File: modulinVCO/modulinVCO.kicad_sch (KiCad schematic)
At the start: 106 parts, among them J1 Conn_01x06_Pin, Q1 BC548, Q2 BC548, Q3 2N7000, Q4 BC548, Q5 BC548, SW1 SW_SPDT, U1 TL074, U2 LM7805, U3 TL074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

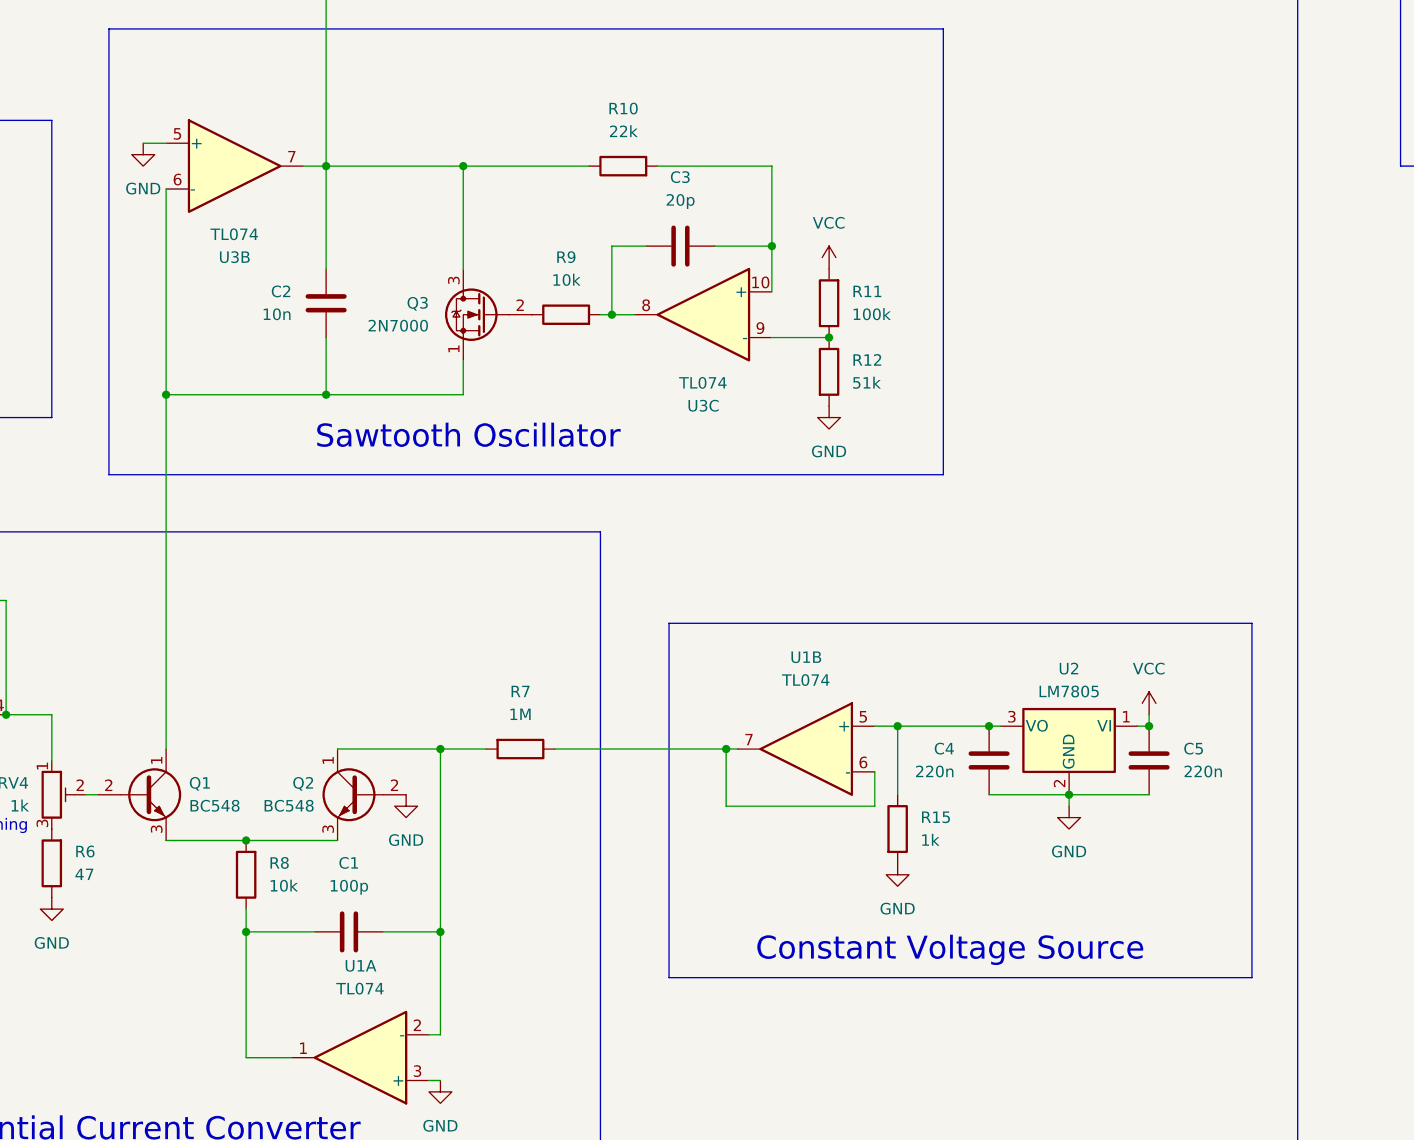
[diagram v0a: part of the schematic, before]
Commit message: Add VCF ciruit and edit for JLCPCB
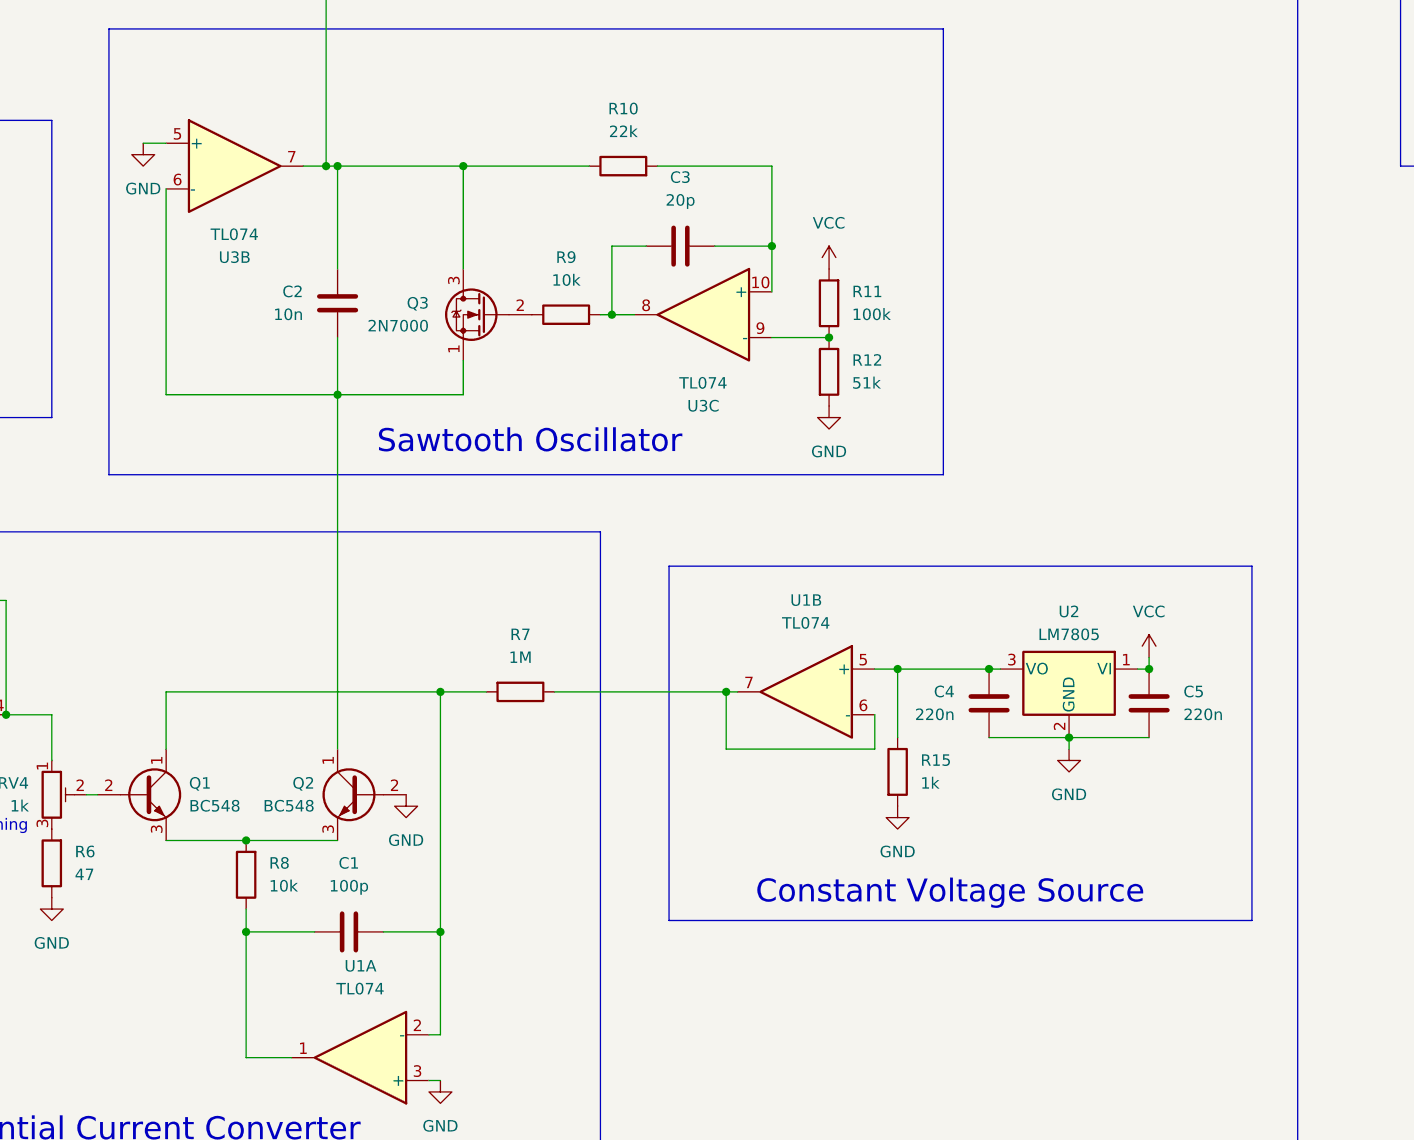
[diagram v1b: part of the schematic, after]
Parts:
- SW1: footprint User:SW_Slide_SPST_H6.00mm_CNC -> User:SW_Slide_SPDT_H6.00mm_CNC
- U7, U8: footprint User:DIP8_CNC -> User:DIP-8_CNC
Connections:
- net at C1.2, R7.2, U1.2 (-): now also Q1.1 (C); no longer Q2.1 (C)
- net at C2.2, Q3.1 (S), U3.6 (-): now also Q2.1 (C); no longer Q1.1 (C)
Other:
- moved on the sheet: C2, C4, C5, R15, R7, U1B, U2

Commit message: Add STEP files
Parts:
- added C10, C11: 100n, User:C_Radial_Polarized_P3.8mm_CNC, symbol Device:C
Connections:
- net GND: now also C10.2, C11.1
- net VCC: now also RV1.3, RV2.3, C10.1; no longer RV1.1, RV2.1
- net VEE: now also RV1.1, RV2.1, C11.2; no longer RV1.3, RV2.3
